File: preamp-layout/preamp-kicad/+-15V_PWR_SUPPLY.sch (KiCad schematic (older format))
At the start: 33 parts, among them J5 Screw_Terminal_01x02, J6 Conn_01x03_Male, J7 Conn_01x03_Male, J8 Conn_01x03_Male, T1 Transformer_1P_1S, U1 L7805, U2 LM7905_TO220

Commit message: Transformer specification
updated schematic, BOM with power transformer info. Other minor schematic tweaks.
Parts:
- removed T1: Transformer_1P_1S, symbol Device:Transformer_1P_1S
- added T1: Transformer_1P_2S, symbol Device:Transformer_1P_2S
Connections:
- wire segments 122 -> 121
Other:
- note added: "+19.2VDC"
- note added: "-19.2VDC"
- note added: "120VAC"
- note added: "28VAC"
- moved on the sheet: C10, C11, C2, C3, C4, C5, C6, C7, C8, C9, D1, D2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

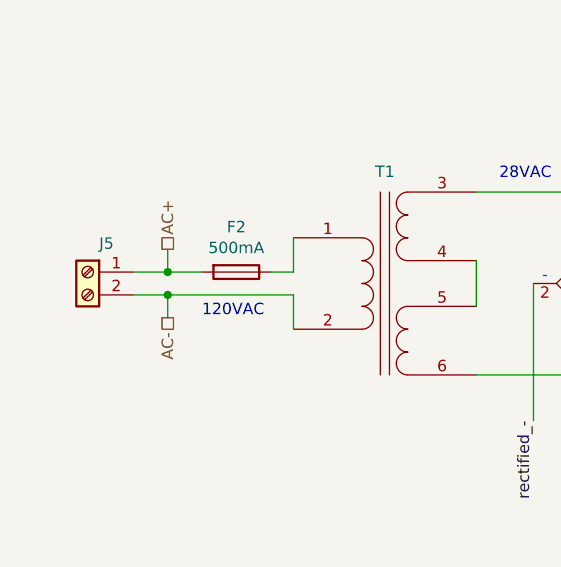
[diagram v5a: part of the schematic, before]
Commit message: screw terminal update
AC power conn update to implement ground. Moved BOM to html file format for web view, not sure if I like it like this but wanted to try it.
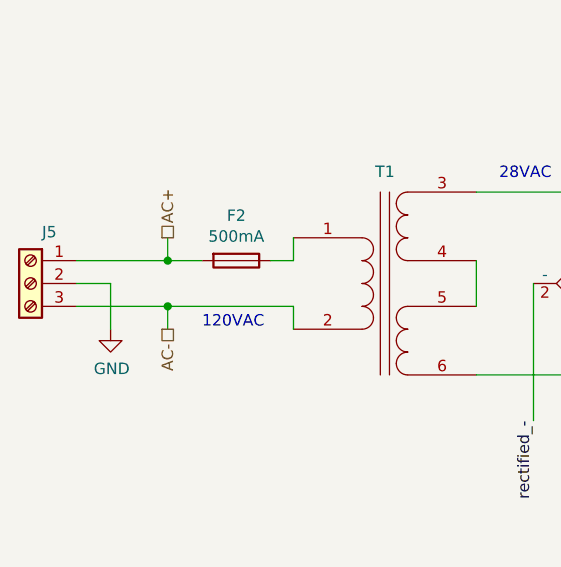
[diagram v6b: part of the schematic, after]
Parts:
- removed J5: Screw_Terminal_01x02, TerminalBlock_Phoenix:TerminalBlock_Phoenix_PT-1,5-2-5.0-H_1x02_P5.00mm_Horizontal, symbol Connector:Screw_Terminal_01x02
- added J5: Screw_Terminal_01x03, TerminalBlock_Phoenix:TerminalBlock_Phoenix_MKDS-3-3-5.08_1x03_P5.08mm_Horizontal, symbol Connector:Screw_Terminal_01x03
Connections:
- net AC+: now also J5.1 (Pin_1)
- net AC-: now also J5.3 (Pin_3)
- net GND: now also J5.2 (Pin_2)
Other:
- moved on the sheet: F2
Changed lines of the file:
@@
 Comment4 "Author: Jordon Gerber"
 $EndDescr
-$Comp
-L Connector:Screw_Terminal_01x02 J5
-U 1 1 5F8FF1B9
-P 1600 3400
-F 0 "J5" H 1518 3525 50  0000 C CNN
-F 1 "Screw_Terminal_01x02" H 1518 3166 50  0001 C CNN
-F 2 "TerminalBlock_Phoenix:TerminalBlock_Phoenix_PT-1,5-2-5.0-H_1x02_P5.00mm_Horizontal" H 1600 3400 50  0001 C CNN
-F 3 "~" H 1600 3400 50  0001 C CNN
-	1    1600 3400
-	-1   0    0    -1
-$EndComp
-Wire Wire Line
-	2500 3400 2500 3250
-Wire Wire Line
-	2500 3500 2500 3650
-Text HLabel 1950 3300 1    50   UnSpc ~ 0
+Text HLabel 1950 3250 1    50   UnSpc ~ 0
 AC+
-Text HLabel 1950 3600 3    50   UnSpc ~ 0
+Text HLabel 1950 3650 3    50   UnSpc ~ 0
 AC-
 Text GLabel 3900 6000 1    50   UnSpc ~ 0
@@
 L Device:Fuse F?
 U 1 1 60029A0D
-P 2250 3400
+P 2250 3350
 AR Path="/5E26F6FE/60029A0D" Ref="F?"  Part="1"
 AR Path="/5E27B612/60029A0D" Ref="F2"  Part="1"
-F 0 "F2" V 2053 3400 50  0000 C CNN
-F 1 "500mA" V 2144 3400 50  0000 C CNN
-F 2 "" V 2180 3400 50  0001 C CNN
-F 3 "~" H 2250 3400 50  0001 C CNN
-	1    2250 3400
+F 0 "F2" V 2053 3350 50  0000 C CNN
+F 1 "500mA" V 2144 3350 50  0000 C CNN
+F 2 "" V 2180 3350 50  0001 C CNN
+F 3 "~" H 2250 3350 50  0001 C CNN
+	1    2250 3350
 	0    1    1    0
 $EndComp
@@
 $EndComp
 Wire Wire Line
-	1800 3400 1950 3400
-Wire Wire Line
-	1800 3500 1950 3500
-Wire Wire Line
-	1950 3300 1950 3400
-Connection ~ 1950 3400
-Wire Wire Line
-	1950 3500 1950 3600
-Connection ~ 1950 3500
-Wire Wire Line
-	1950 3400 2100 3400
-Wire Wire Line
-	1950 3500 2500 3500
-Wire Wire Line
-	2400 3400 2500 3400
+	1950 3250 1950 3350
+Connection ~ 1950 3350
+Wire Wire Line
+	1950 3550 1950 3650
+Connection ~ 1950 3550
+Wire Wire Line
+	1950 3350 2100 3350
+Wire Wire Line
+	1950 3550 2500 3550
+Wire Wire Line
+	2400 3350 2500 3350
 Wire Wire Line
 	3850 3150 3850 3050
@@
 Wire Wire Line
 	3850 3750 3850 3850
-Text Notes 2100 3600 0    50   ~ 0
+Text Notes 2100 3650 0    50   ~ 0
 120VAC
 Text Notes 3400 3000 0    50   ~ 0
@@
 Text Notes 6800 4900 0    50   ~ 0
 -19.2VDC
+$Comp
+L Connector:Screw_Terminal_01x03 J?
+U 1 1 5E8FCAF8
+P 1350 3450
+AR Path="/5E26F6FE/5E8FCAF8" Ref="J?"  Part="1"
+AR Path="/5E5EF2D4/5E8FCAF8" Ref="J?"  Part="1"
+AR Path="/5E27B612/5E8FCAF8" Ref="J5"  Part="1"
+F 0 "J5" H 1268 3675 50  0000 C CNN
+F 1 "Screw_Terminal_01x03" H 1268 3216 50  0001 C CNN
+F 2 "TerminalBlock_Phoenix:TerminalBlock_Phoenix_MKDS-3-3-5.08_1x03_P5.08mm_Horizontal" H 1350 3450 50  0001 C CNN
+F 3 "~" H 1350 3450 50  0001 C CNN
+	1    1350 3450
+	-1   0    0    -1
+$EndComp
+Wire Wire Line
+	2500 3350 2500 3250
+Wire Wire Line
+	2500 3550 2500 3650
+$Comp
+L power:GND #PWR?
+U 1 1 5E92CBD9
+P 1700 3650
+AR Path="/5E26F6FE/5E92CBD9" Ref="#PWR?"  Part="1"
+AR Path="/5E27B612/5E92CBD9" Ref="#PWR?"  Part="1"
+F 0 "#PWR?" H 1700 3400 50  0001 C CNN
+F 1 "GND" H 1705 3477 50  0000 C CNN
+F 2 "" H 1700 3650 50  0001 C CNN
+F 3 "" H 1700 3650 50  0001 C CNN
+	1    1700 3650
+	1    0    0    -1
+$EndComp
+Wire Wire Line
+	1550 3450 1700 3450
+Wire Wire Line
+	1700 3450 1700 3650
+Wire Wire Line
+	1550 3550 1950 3550
+Wire Wire Line
+	1550 3350 1950 3350
 $EndSCHEMATC

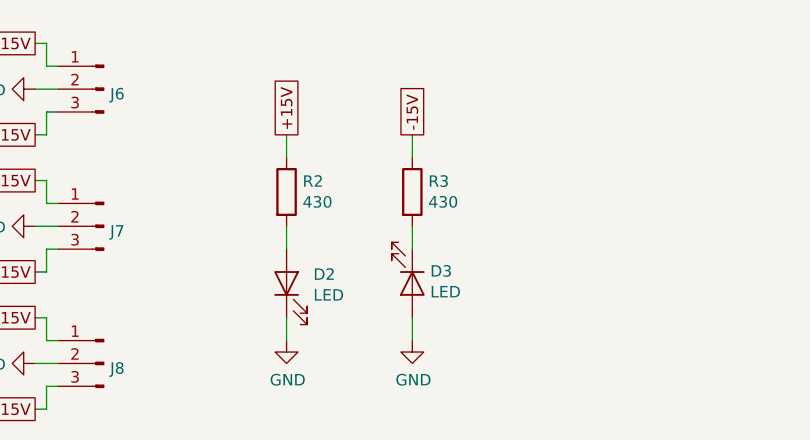
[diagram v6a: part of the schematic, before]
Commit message: Added front panel LED sheet. BOM update. Front panel PCA work
other minor changes like LED color assignments, etc
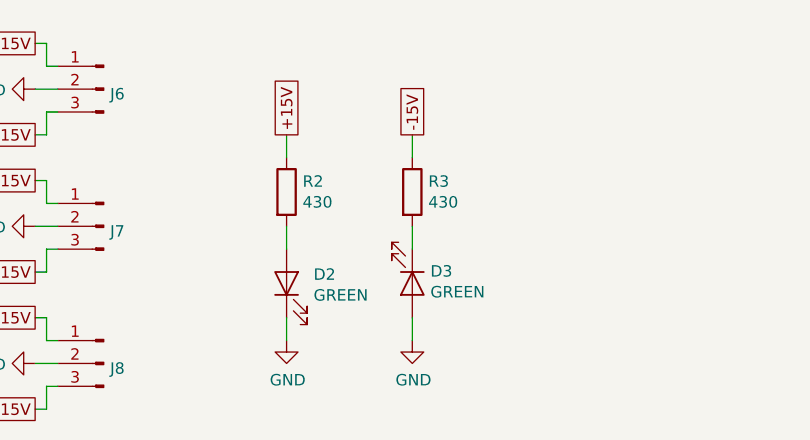
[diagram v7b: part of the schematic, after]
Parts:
- D2, D3: value LED -> GREEN
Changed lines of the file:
@@
 $Descr A4 11693 8268
 encoding utf-8
-Sheet 3 11
+Sheet 3 12
 Title "15V Power Supply"
 Date "2020-01-23"
@@
 AR Path="/5E2D8DA2/5FFF1136" Ref="D?"  Part="1"
 AR Path="/5E27B612/5FFF1136" Ref="D2"  Part="1"
-F 0 "D2" V 3939 6533 50  0000 R CNN
-F 1 "LED" V 3848 6533 50  0000 R CNN
+F 0 "D2" V 3939 6532 50  0000 R CNN
+F 1 "GREEN" V 3848 6532 50  0000 R CNN
 F 2 "LED_SMD:LED_1206_3216Metric_Pad1.42x1.75mm_HandSolder" H 3900 6650 50  0001 C CNN
 F 3 "~" H 3900 6650 50  0001 C CNN
@@
 AR Path="/5E2D8DA2/5FFF114C" Ref="D?"  Part="1"
 AR Path="/5E27B612/5FFF114C" Ref="D3"  Part="1"
-F 0 "D3" V 4397 6728 50  0000 L CNN
-F 1 "LED" V 4488 6728 50  0000 L CNN
+F 0 "D3" V 4397 6729 50  0000 L CNN
+F 1 "GREEN" V 4488 6729 50  0000 L CNN
 F 2 "LED_SMD:LED_1206_3216Metric_Pad1.42x1.75mm_HandSolder" H 4450 6650 50  0001 C CNN
 F 3 "~" H 4450 6650 50  0001 C CNN
@@
 P 1700 3650
 AR Path="/5E26F6FE/5E92CBD9" Ref="#PWR?"  Part="1"
-AR Path="/5E27B612/5E92CBD9" Ref="#PWR?"  Part="1"
-F 0 "#PWR?" H 1700 3400 50  0001 C CNN
+AR Path="/5E27B612/5E92CBD9" Ref="#PWR0112"  Part="1"
+F 0 "#PWR0112" H 1700 3400 50  0001 C CNN
 F 1 "GND" H 1705 3477 50  0000 C CNN
 F 2 "" H 1700 3650 50  0001 C CNN

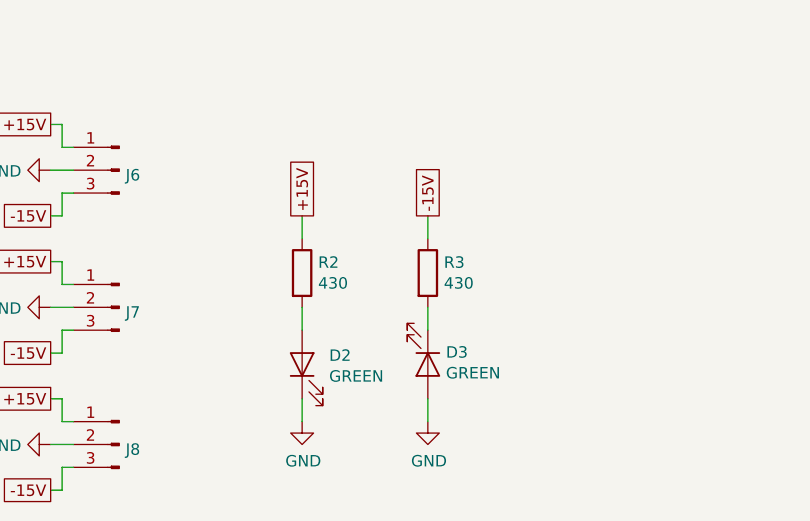
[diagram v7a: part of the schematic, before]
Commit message: LED resistor update
In the process of reviewing layouts and associated parts sourcing, I realized that I had incorrectly calculated the resistors needed for the power supply LEDs on all boards. Updated BOM and schematics to match. Other minor schematic updates.
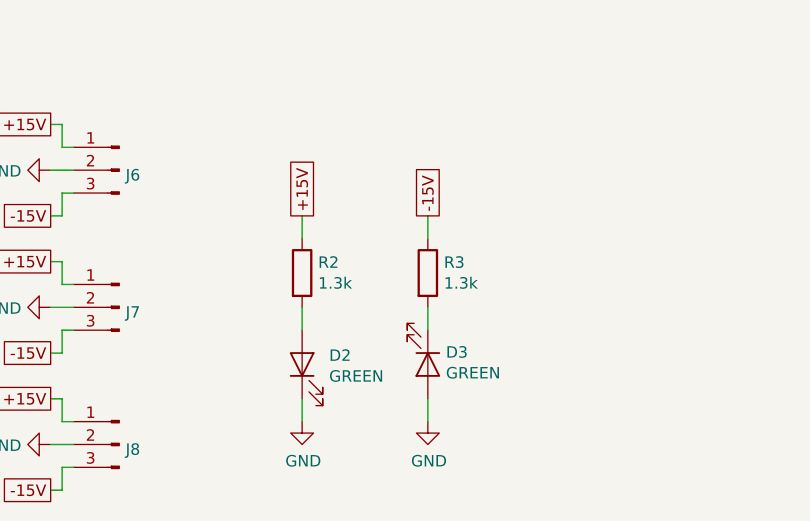
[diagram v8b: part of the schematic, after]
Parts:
- R2, R3: value 430 -> 1.3k
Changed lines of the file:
@@
 AR Path="/5E27B612/5FFF1130" Ref="R2"  Part="1"
 F 0 "R2" H 3970 6296 50  0000 L CNN
-F 1 "430" H 3970 6205 50  0000 L CNN
+F 1 "1.3k" H 3970 6205 50  0000 L CNN
 F 2 "Resistor_SMD:R_1206_3216Metric_Pad1.42x1.75mm_HandSolder" V 3830 6250 50  0001 C CNN
 F 3 "~" H 3900 6250 50  0001 C CNN
@@
 AR Path="/5E27B612/5FFF1146" Ref="R3"  Part="1"
 F 0 "R3" H 4520 6296 50  0000 L CNN
-F 1 "430" H 4520 6205 50  0000 L CNN
+F 1 "1.3k" H 4520 6205 50  0000 L CNN
 F 2 "Resistor_SMD:R_1206_3216Metric_Pad1.42x1.75mm_HandSolder" V 4380 6250 50  0001 C CNN
 F 3 "~" H 4450 6250 50  0001 C CNN
